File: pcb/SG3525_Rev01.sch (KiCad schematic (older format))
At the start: 21 parts, among them J1 Conn_01x06, U1 SG3525

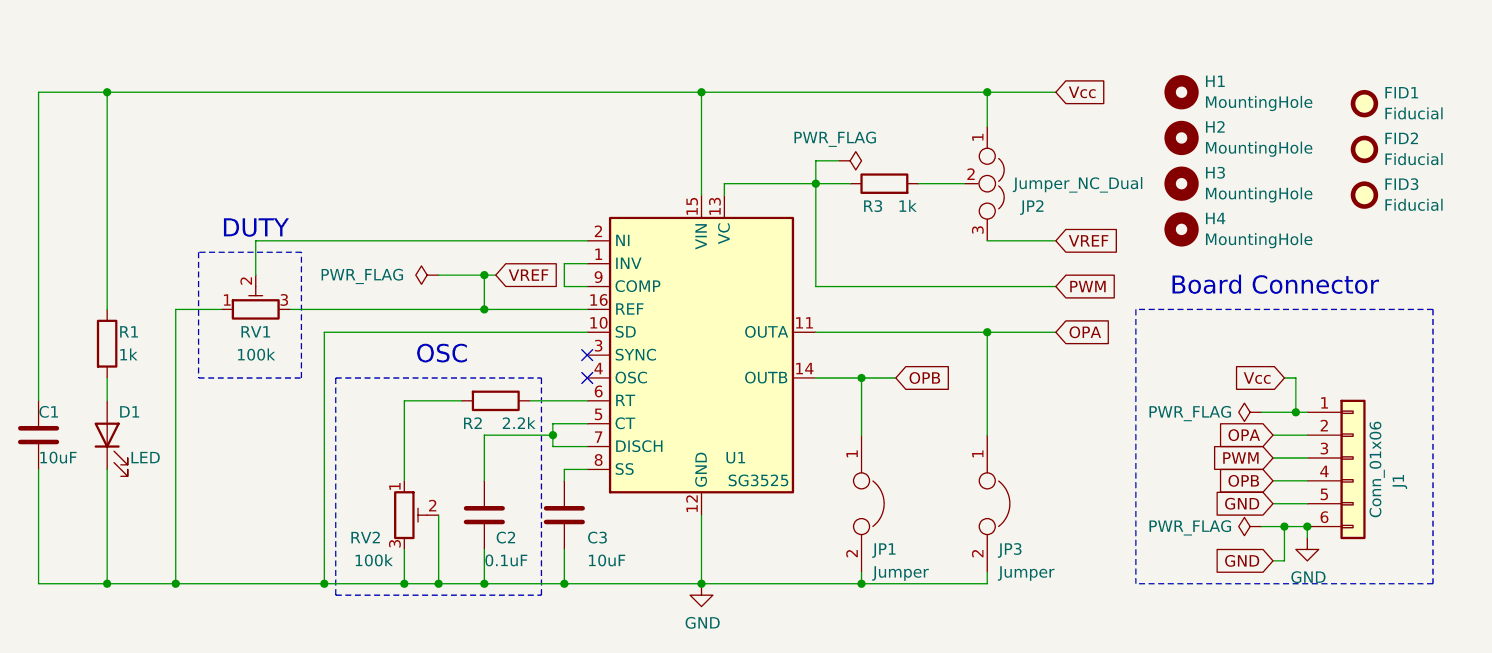
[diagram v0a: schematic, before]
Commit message: Correct global labels for locals
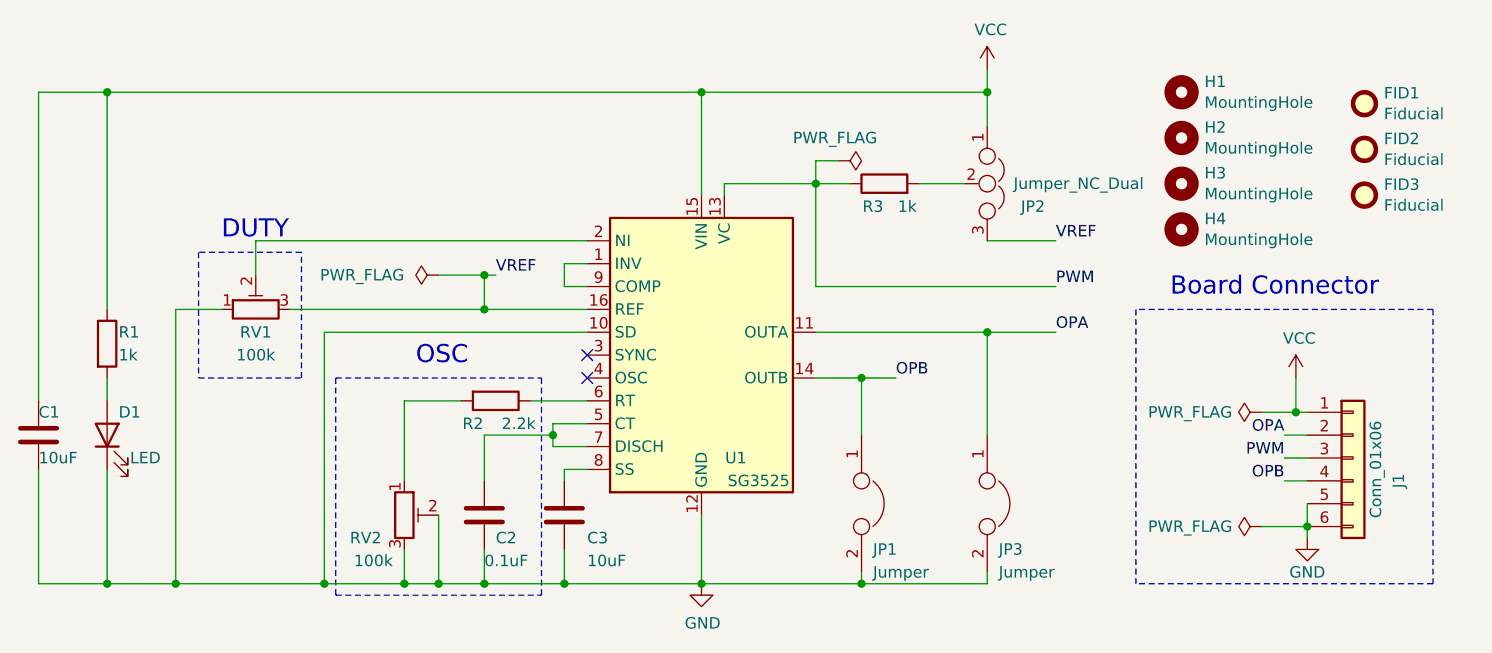
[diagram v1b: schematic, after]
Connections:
- net Vcc renamed VCC
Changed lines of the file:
@@
 	2850 4800 3150 4800
 Connection ~ 3150 4800
-Text GLabel 7300 3500 2    50   Input ~ 0
-PWM
 Wire Wire Line
 	5750 2650 7000 2650
@@
 Wire Wire Line
 	6250 3500 7300 3500
-Text GLabel 7300 3700 2    50   Input ~ 0
-OPA
 Connection ~ 7000 3700
-Text GLabel 6600 3900 2    50   Input ~ 0
-OPB
 Wire Wire Line
 	6600 3900 6450 3900
@@
 Wire Wire Line
 	7000 3700 7300 3700
-Text GLabel 7300 3300 2    50   Input ~ 0
-VREF
 Wire Wire Line
 	7000 3300 7300 3300
-Text GLabel 4850 3450 2    50   Input ~ 0
-VREF
 Wire Wire Line
 	4850 3450 4800 3450
@@
 Wire Wire Line
 	4450 4350 4450 4000
-Text GLabel 7300 2650 2    50   Input ~ 0
-Vcc
-Wire Wire Line
-	7300 2650 7000 2650
 Connection ~ 7000 2650
 NoConn ~ 5250 3900
@@
 Wire Wire Line
 	6350 2950 6250 2950
-Wire Wire Line
-	8250 4150 8400 4150
-Wire Wire Line
-	8250 4250 8400 4250
-Wire Wire Line
-	8250 4350 8400 4350
-Wire Wire Line
-	8250 4450 8400 4450
-Text GLabel 8250 4450 0    50   Input ~ 0
-GND
-Text GLabel 8250 4700 0    50   Input ~ 0
-GND
-Text GLabel 8250 4250 0    50   Input ~ 0
-PWM
-Text GLabel 8250 4350 0    50   Input ~ 0
-OPB
-Text GLabel 8250 4150 0    50   Input ~ 0
-OPA
-Text GLabel 8300 3900 0    50   Input ~ 0
-Vcc
 $Comp
 L power:PWR_FLAG #FLG02
@@
 Wire Wire Line
 	8200 4050 8350 4050
-Wire Wire Line
-	8200 4550 8300 4550
 $Comp
 L power:GND #PWR03
@@
 P 8400 4600
 F 0 "#PWR03" H 8400 4350 50  0001 C CNN
-F 1 "GND" H 8405 4427 50  0000 C CNN
+F 1 "GND" H 8400 4450 50  0000 C CNN
 F 2 "" H 8400 4600 50  0001 C CNN
 F 3 "" H 8400 4600 50  0001 C CNN
@@
 	8400 4600 8400 4550
 Connection ~ 8400 4550
-Wire Wire Line
-	8250 4700 8300 4700
-Wire Wire Line
-	8300 4700 8300 4550
-Connection ~ 8300 4550
-Wire Wire Line
-	8300 4550 8400 4550
-Wire Wire Line
-	8300 3900 8350 3900
 Wire Wire Line
 	8350 3900 8350 4050
@@
 	1    0    0    -1
 $EndComp
+$Comp
+L power:VCC #PWR0101
+U 1 1 614C3DD8
+P 7000 2550
+F 0 "#PWR0101" H 7000 2400 50  0001 C CNN
+F 1 "VCC" H 7015 2723 50  0000 C CNN
+F 2 "" H 7000 2550 50  0001 C CNN
+F 3 "" H 7000 2550 50  0001 C CNN
+	1    7000 2550
+	1    0    0    -1
+$EndComp
+Wire Wire Line
+	7000 2550 7000 2650
+Wire Wire Line
+	8200 4550 8400 4550
+Wire Wire Line
+	8400 4450 8400 4550
+Text Label 8300 4350 2    50   ~ 0
+OPB
+Text Label 8300 4250 2    50   ~ 0
+PWM
+Text Label 8300 4150 2    50   ~ 0
+OPA
+Wire Wire Line
+	8400 4150 8300 4150
+Wire Wire Line
+	8400 4250 8300 4250
+Wire Wire Line
+	8400 4350 8300 4350
+Text Label 7300 3700 0    50   ~ 0
+OPA
+Text Label 7300 3500 0    50   ~ 0
+PWM
+Text Label 6600 3900 0    50   ~ 0
+OPB
+Text Label 7300 3300 0    50   ~ 0
+VREF
+Text Label 4850 3450 0    50   ~ 0
+VREF
+$Comp
+L power:VCC #PWR0102
+U 1 1 614E8B62
+P 8350 3900
+F 0 "#PWR0102" H 8350 3750 50  0001 C CNN
+F 1 "VCC" H 8365 4073 50  0000 C CNN
+F 2 "" H 8350 3900 50  0001 C CNN
+F 3 "" H 8350 3900 50  0001 C CNN
+	1    8350 3900
+	1    0    0    -1
+$EndComp

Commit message: Last changes after .sch presentation
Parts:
- C1: Manufacture Part (none) -> T95V155K035HSSL; Manufacture Product Number T95V155K035HSSL -> (none)
- U1: Manufacture Part (none) -> SG3525AP013TR
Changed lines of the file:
@@
 F 2 "Package_SO:SOP-16_4.4x10.4mm_P1.27mm" H 5750 3800 50  0001 C CNN
 F 3 "www.st.com/resource/en/datasheet/sg3525.pdf" H 5750 3800 50  0001 C CNN
+F 4 "SG3525AP013TR" H 5750 3800 50  0001 C CNN "Manufacture Part"
 	1    5750 3800
 	1    0    0    -1
@@
 F 2 "Capacitor_Tantalum_SMD:CP_EIA-1608-10_AVX-L" H 2888 4000 50  0001 C CNN
 F 3 "https://www.digikey.com/en/products/detail/vishay-sprague/T95V155K035HSSL/2808151" H 2850 4150 50  0001 C CNN
-F 4 "T95V155K035HSSL" H 2850 4150 50  0001 C CNN "Manufacture Product Number"
+F 4 "" H 2850 4150 50  0001 C CNN "Manufacture Product Number"
+F 5 "T95V155K035HSSL" H 2850 4150 50  0001 C CNN "Manufacture Part"
 	1    2850 4150
 	1    0    0    -1
